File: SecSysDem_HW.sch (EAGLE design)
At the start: 47 parts, among them J1 22-05-7078-07, J2 22-27-2021-02, Q1 2N3904, T1 MOSFET_NCHANNEL_ENHANCEMENT2N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, T2 MOSFET_NCHANNEL_ENHANCEMENT2N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, T3 MOSFET_NCHANNEL_ENHANCEMENT2N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, U1 XPLAINED_MINI_PINOUT, U2 PCF8574_IO_EXPANDER, U3 MCP4706_DAC, U4 FT24C512A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

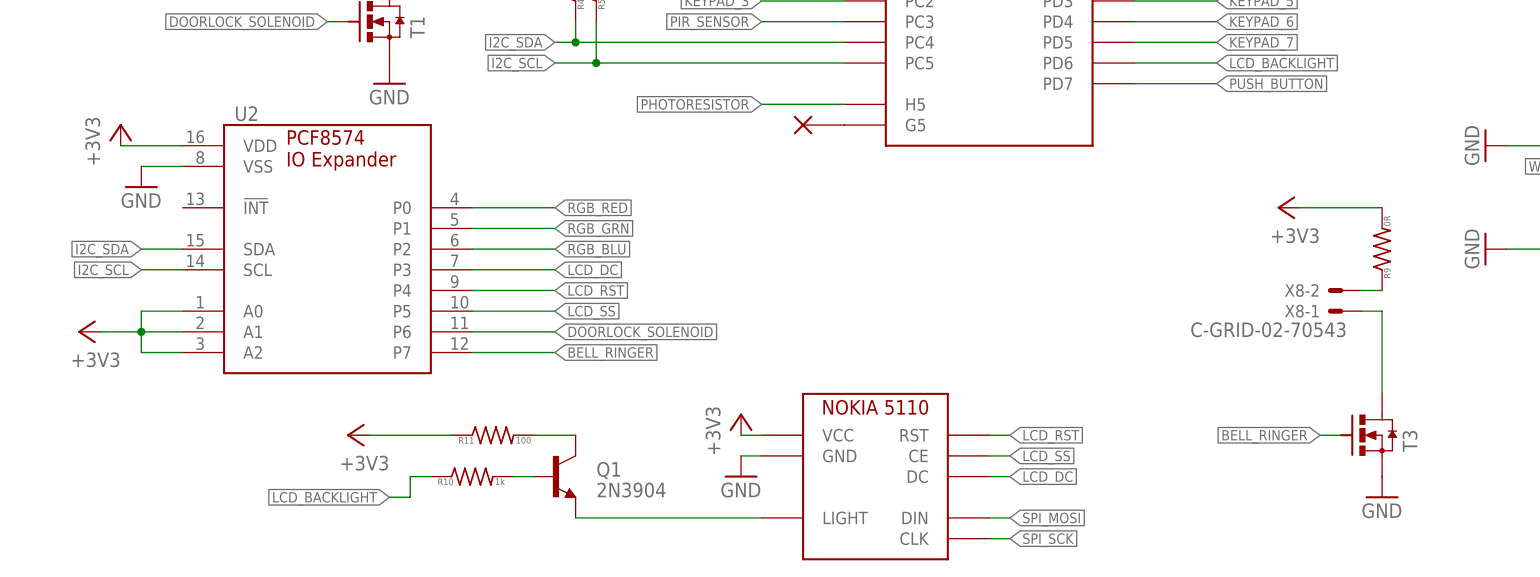
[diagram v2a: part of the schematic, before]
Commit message: Started the pcb layout. PCB made to fit the TaydaElectronics.com plastic box
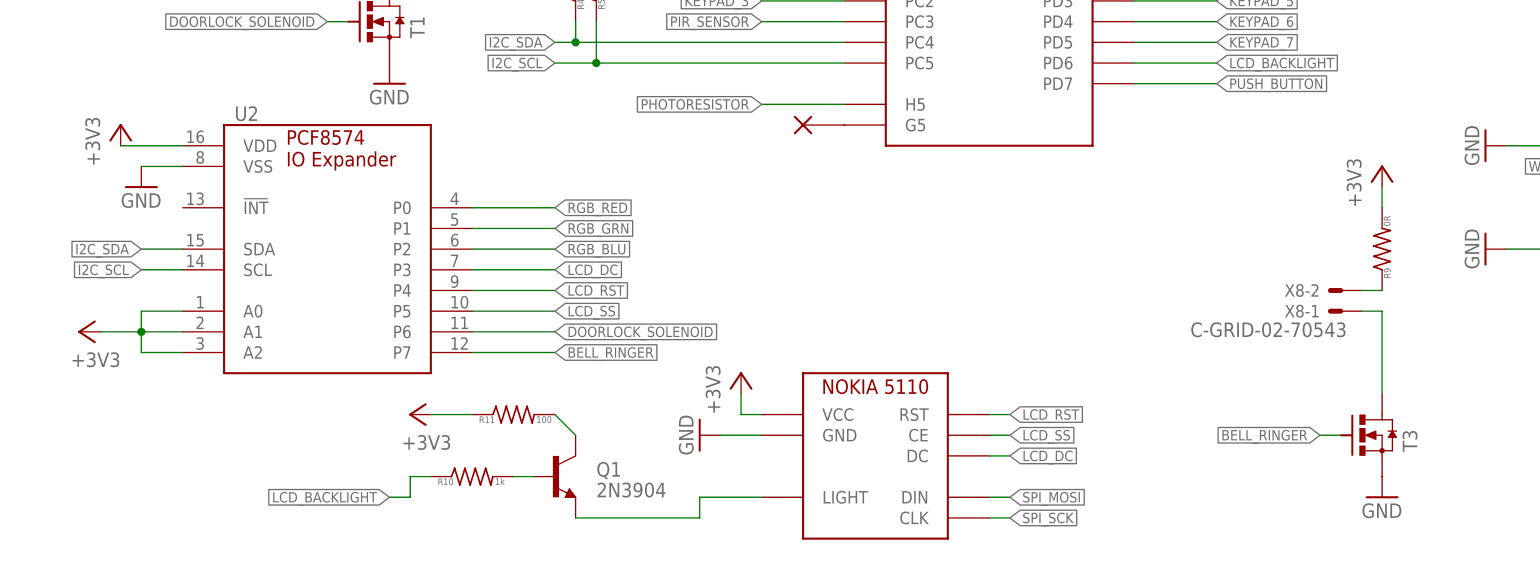
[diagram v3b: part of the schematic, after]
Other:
- moved on the sheet: R11
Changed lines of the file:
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@@
 <instance part="GND10" gate="1" x="185.42" y="55.88" rot="R270"/>
 <instance part="GND11" gate="1" x="185.42" y="43.18" rot="R270"/>
-<instance part="U$3" gate="G$1" x="101.6" y="5.08"/>
-<instance part="GND12" gate="1" x="93.98" y="15.24"/>
-<instance part="+3V4" gate="G$1" x="93.98" y="22.86"/>
+<instance part="U$3" gate="G$1" x="101.6" y="7.62"/>
+<instance part="GND12" gate="1" x="88.9" y="20.32" rot="R270"/>
+<instance part="+3V4" gate="G$1" x="93.98" y="27.94"/>
 <instance part="X4" gate="-1" x="226.06" y="127"/>
 <instance part="X4" gate="-2" x="226.06" y="124.46"/>
@@
 <instance part="X8" gate="-1" x="167.64" y="35.56" rot="R180"/>
 <instance part="R9" gate="G$1" x="172.72" y="43.18" rot="R90"/>
-<instance part="+3V10" gate="G$1" x="160.02" y="48.26" rot="R90"/>
+<instance part="+3V10" gate="G$1" x="172.72" y="53.34"/>
 <instance part="V2" gate="G$1" x="147.32" y="93.98"/>
 <instance part="V3" gate="G$1" x="147.32" y="81.28"/>
@@
 <instance part="+3V11" gate="G$1" x="218.44" y="162.56"/>
 <instance part="Q1" gate="G$1" x="71.12" y="15.24"/>
-<instance part="+3V12" gate="G$1" x="45.72" y="20.32" rot="R90"/>
+<instance part="+3V12" gate="G$1" x="53.34" y="22.86" rot="R90"/>
 <instance part="R10" gate="G$1" x="60.96" y="15.24"/>
-<instance part="R11" gate="G$1" x="63.5" y="20.32"/>
+<instance part="R11" gate="G$1" x="66.04" y="22.86"/>
 <instance part="+3V13" gate="G$1" x="12.7" y="33.02" rot="R90"/>
 </instances>
@@
 <segment>
 <pinref part="U$3" gate="G$1" pin="GND"/>
-<wire x1="96.52" y1="17.78" x2="93.98" y2="17.78" width="0.1524" layer="91"/>
+<wire x1="96.52" y1="20.32" x2="91.44" y2="20.32" width="0.1524" layer="91"/>
 <pinref part="GND12" gate="1" pin="GND"/>
 </segment>
@@
 <segment>
 <pinref part="U$3" gate="G$1" pin="CLK"/>
-<wire x1="124.46" y1="7.62" x2="127" y2="7.62" width="0.1524" layer="91"/>
-<label x="127" y="7.62" size="1.27" layer="95" xref="yes"/>
+<wire x1="124.46" y1="10.16" x2="127" y2="10.16" width="0.1524" layer="91"/>
+<label x="127" y="10.16" size="1.27" layer="95" xref="yes"/>
 </segment>
 </net>
@@
 <segment>
 <pinref part="U$3" gate="G$1" pin="DIN"/>
-<wire x1="124.46" y1="10.16" x2="127" y2="10.16" width="0.1524" layer="91"/>
-<label x="127" y="10.16" size="1.27" layer="95" xref="yes"/>
+<wire x1="124.46" y1="12.7" x2="127" y2="12.7" width="0.1524" layer="91"/>
+<label x="127" y="12.7" size="1.27" layer="95" xref="yes"/>
 </segment>
 </net>
@@
 <segment>
 <pinref part="U$3" gate="G$1" pin="VCC"/>
-<wire x1="96.52" y1="20.32" x2="93.98" y2="20.32" width="0.1524" layer="91"/>
+<wire x1="96.52" y1="22.86" x2="93.98" y2="22.86" width="0.1524" layer="91"/>
+<wire x1="93.98" y1="22.86" x2="93.98" y2="25.4" width="0.1524" layer="91"/>
 <pinref part="+3V4" gate="G$1" pin="+3V3"/>
 </segment>
@@
 <pinref part="R9" gate="G$1" pin="2"/>
 <pinref part="+3V10" gate="G$1" pin="+3V3"/>
-<wire x1="162.56" y1="48.26" x2="172.72" y2="48.26" width="0.1524" layer="91"/>
+<wire x1="172.72" y1="50.8" x2="172.72" y2="48.26" width="0.1524" layer="91"/>
 </segment>
 <segment>
@@
 <pinref part="R11" gate="G$1" pin="1"/>
 <pinref part="+3V12" gate="G$1" pin="+3V3"/>
-<wire x1="58.42" y1="20.32" x2="48.26" y2="20.32" width="0.1524" layer="91"/>
+<wire x1="60.96" y1="22.86" x2="55.88" y2="22.86" width="0.1524" layer="91"/>
 </segment>
 <segment>
@@
 <wire x1="20.32" y1="33.02" x2="20.32" y2="30.48" width="0.1524" layer="91"/>
 <junction x="20.32" y="33.02"/>
+<wire x1="20.32" y1="33.02" x2="15.24" y2="33.02" width="0.1524" layer="91"/>
 <pinref part="+3V13" gate="G$1" pin="+3V3"/>
-<wire x1="15.24" y1="33.02" x2="20.32" y2="33.02" width="0.1524" layer="91"/>
 </segment>
 </net>
@@
 <pinref part="U$3" gate="G$1" pin="LIGHT"/>
 <pinref part="Q1" gate="G$1" pin="E"/>
-<wire x1="96.52" y1="10.16" x2="73.66" y2="10.16" width="0.1524" layer="91"/>
+<wire x1="96.52" y1="12.7" x2="88.9" y2="12.7" width="0.1524" layer="91"/>
+<wire x1="88.9" y1="12.7" x2="88.9" y2="10.16" width="0.1524" layer="91"/>
+<wire x1="88.9" y1="10.16" x2="73.66" y2="10.16" width="0.1524" layer="91"/>
 </segment>
 <segment>
@@
 <segment>
 <pinref part="U$3" gate="G$1" pin="DC"/>
-<wire x1="124.46" y1="15.24" x2="127" y2="15.24" width="0.1524" layer="91"/>
-<label x="127" y="15.24" size="1.27" layer="95" xref="yes"/>
+<wire x1="124.46" y1="17.78" x2="127" y2="17.78" width="0.1524" layer="91"/>
+<label x="127" y="17.78" size="1.27" layer="95" xref="yes"/>
 </segment>
 </net>
@@
 <segment>
 <pinref part="U$3" gate="G$1" pin="RST"/>
-<wire x1="124.46" y1="20.32" x2="127" y2="20.32" width="0.1524" layer="91"/>
-<label x="127" y="20.32" size="1.27" layer="95" xref="yes"/>
+<wire x1="124.46" y1="22.86" x2="127" y2="22.86" width="0.1524" layer="91"/>
+<label x="127" y="22.86" size="1.27" layer="95" xref="yes"/>
 </segment>
 </net>
@@
 <segment>
 <pinref part="U$3" gate="G$1" pin="CE"/>
-<wire x1="124.46" y1="17.78" x2="127" y2="17.78" width="0.1524" layer="91"/>
-<label x="127" y="17.78" size="1.27" layer="95" xref="yes"/>
+<wire x1="124.46" y1="20.32" x2="127" y2="20.32" width="0.1524" layer="91"/>
+<label x="127" y="20.32" size="1.27" layer="95" xref="yes"/>
 </segment>
 </net>
@@
 <pinref part="Q1" gate="G$1" pin="C"/>
 <pinref part="R11" gate="G$1" pin="2"/>
-<wire x1="73.66" y1="20.32" x2="68.58" y2="20.32" width="0.1524" layer="91"/>
-</segment>
-</net>
+<wire x1="73.66" y1="20.32" x2="71.12" y2="22.86" width="0.1524" layer="91"/>
+</segment>
+</net>

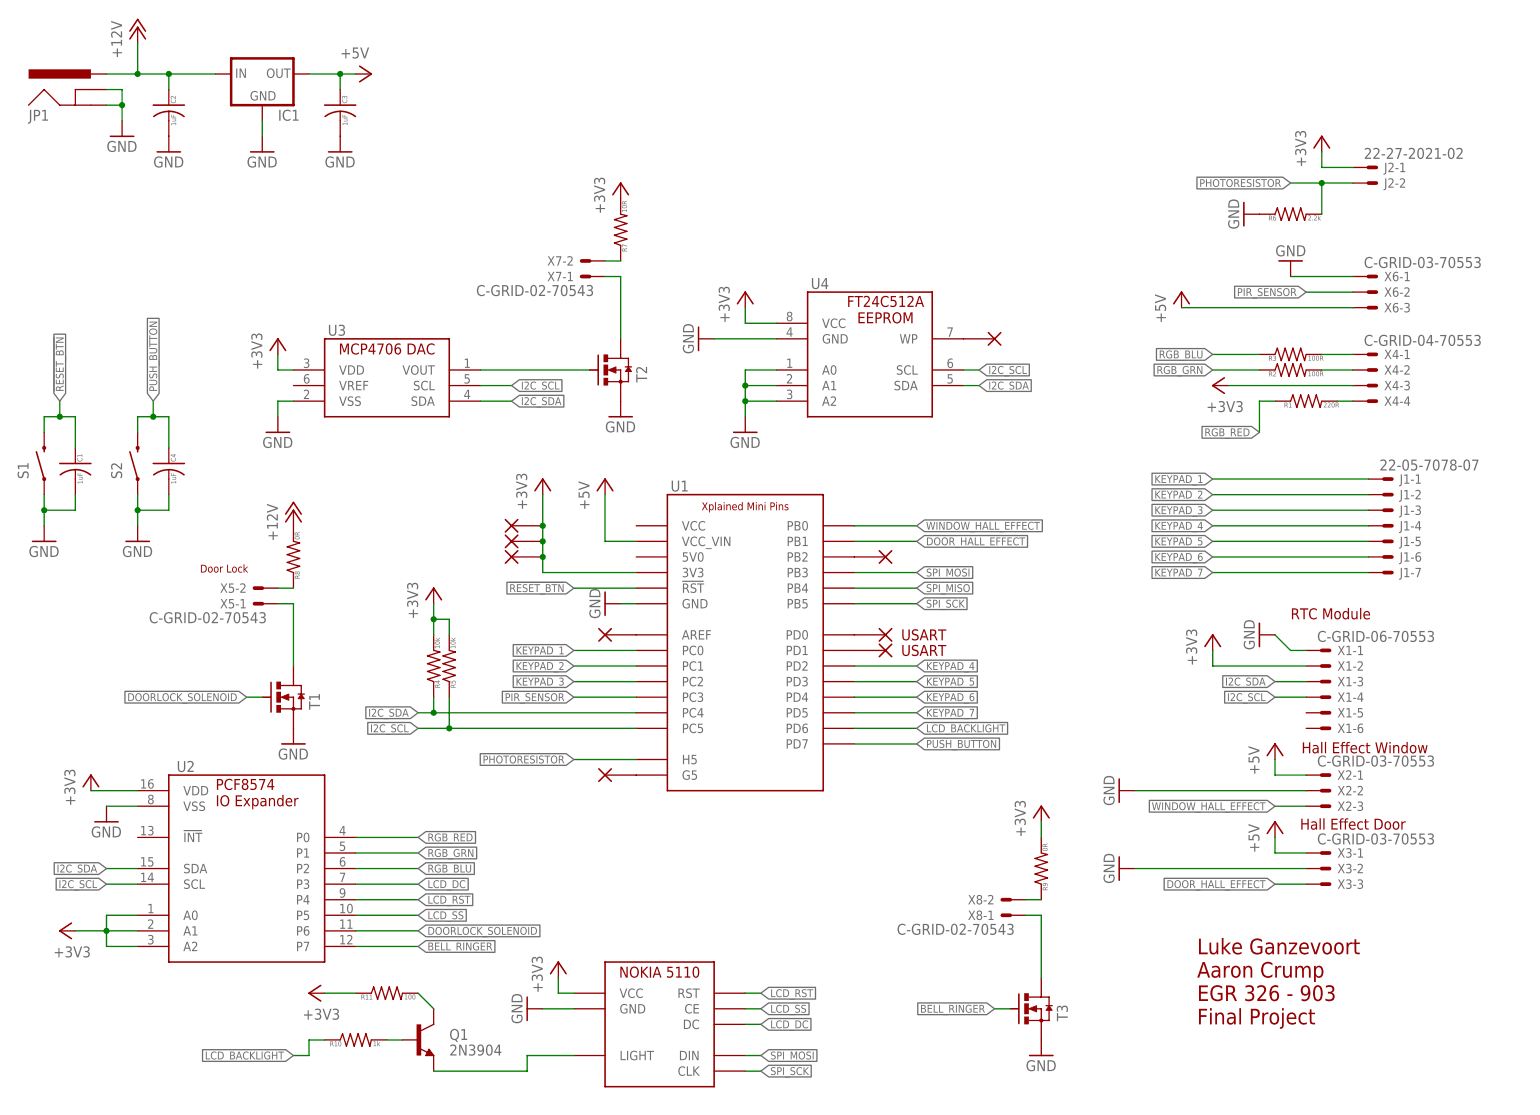
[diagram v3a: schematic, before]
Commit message: Added flyback diode to solenoid. Changed most connectors to verticle. Continued PCB layout and increased PCB size.
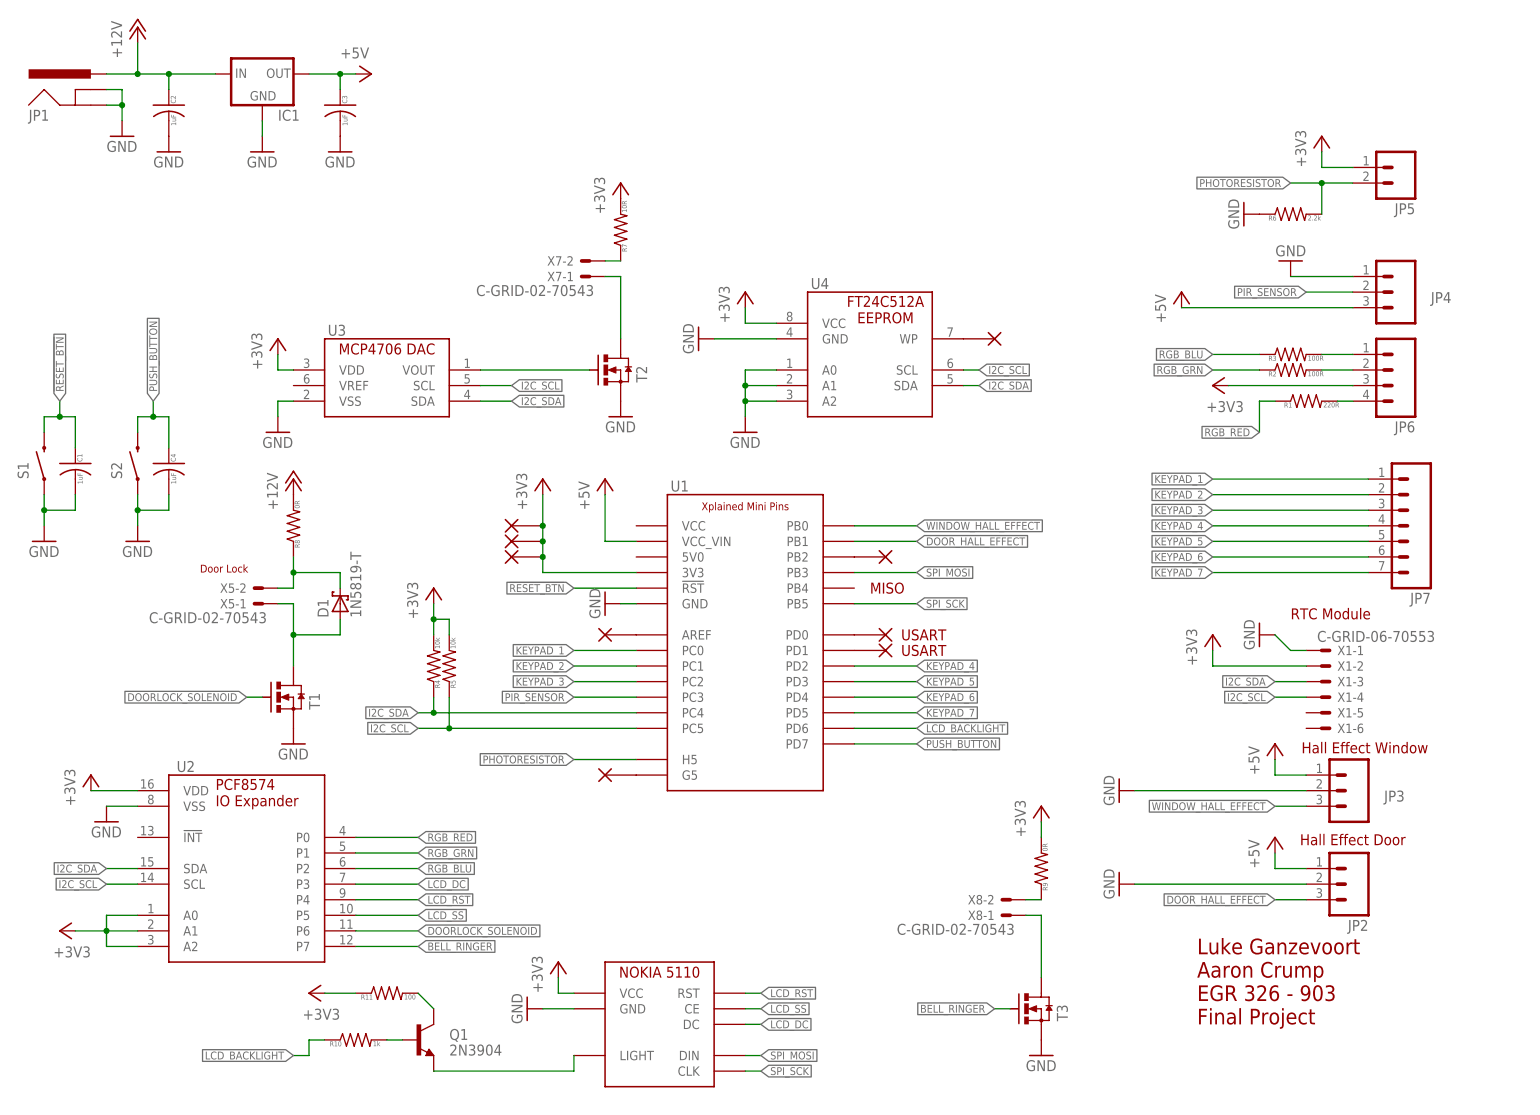
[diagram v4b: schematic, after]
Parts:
- removed J1: 22-05-7078-07, con-molex:22-05-7078-07
- removed J2: 22-27-2021-02, con-molex:22-27-2021-02
- removed X2, X3, X6: C-GRID-03-70553, con-molex:C-GRID-03-70553
- removed X4: C-GRID-04-70553, con-molex:C-GRID-04-70553
- added D1: 1N5819-T, diode:1N5819-T
- added JP2, JP3, JP4: (no value), SparkFun-Connectors:M03PTH
- added JP5: (no value), SparkFun-Connectors:M02PTH
- added JP6: (no value), SparkFun-Connectors:M04PTH
- added JP7: (no value), SparkFun-Connectors:M07
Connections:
- removed net SPI_MISO: U1.PB4
- new net N$19: Q1.E, U$3.LIGHT
- net +3V3: now also JP5.1, JP6.3; no longer J2-1.S, X4-3.S
- net +5V: now also JP2.1, JP3.1, JP4.3; no longer X2-1.S, X3-1.S, X6-3.S
- net DOOR_HALL_EFFECT: now also JP2.3; no longer X3-3.S
- net GND: now also JP2.2, JP3.2, JP4.1; no longer X2-2.S, X3-2.S, X6-1.S
- net KEYPAD_1: now also JP7.1; no longer J1-1.S
- net KEYPAD_2: now also JP7.2; no longer J1-2.S
- net KEYPAD_3: now also JP7.3; no longer J1-3.S
- net KEYPAD_4: now also JP7.4; no longer J1-4.S
- net KEYPAD_5: now also JP7.5; no longer J1-5.S
- net KEYPAD_6: now also JP7.6; no longer J1-6.S
- net KEYPAD_7: now also JP7.7; no longer J1-7.S
- net LCD_BACKLIGHT: no longer Q1.E, U$3.LIGHT
- net N$1: now also D1.A
- net N$17: now also D1.C
- net N$2: now also JP6.4; no longer X4-4.S
- net N$4: now also JP6.2; no longer X4-2.S
- net N$5: now also JP6.1; no longer X4-1.S
- net PHOTORESISTOR: now also JP5.2; no longer J2-2.S
- net PIR_SENSOR: now also JP4.2; no longer X6-2.S
- net WINDOW_HALL_EFFECT: now also JP3.3; no longer X2-3.S
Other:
- note added: "MISO"
- moved on the sheet: R8
